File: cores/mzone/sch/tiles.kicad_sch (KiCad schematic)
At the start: 38 parts

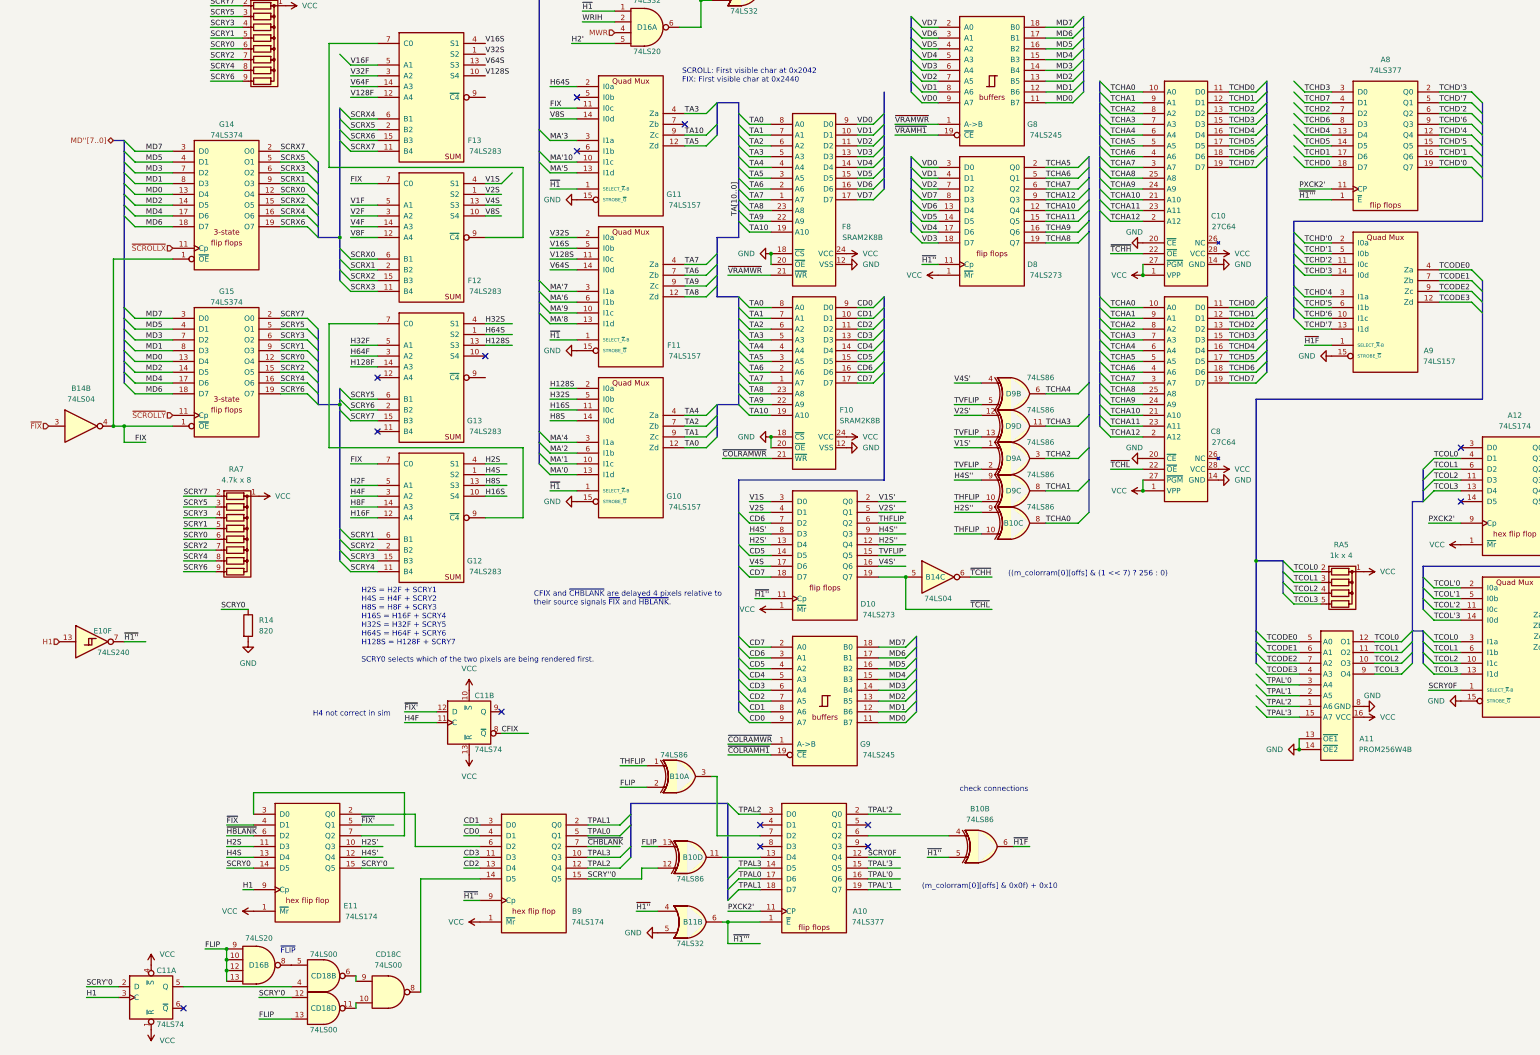
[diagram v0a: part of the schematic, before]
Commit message: mzone core
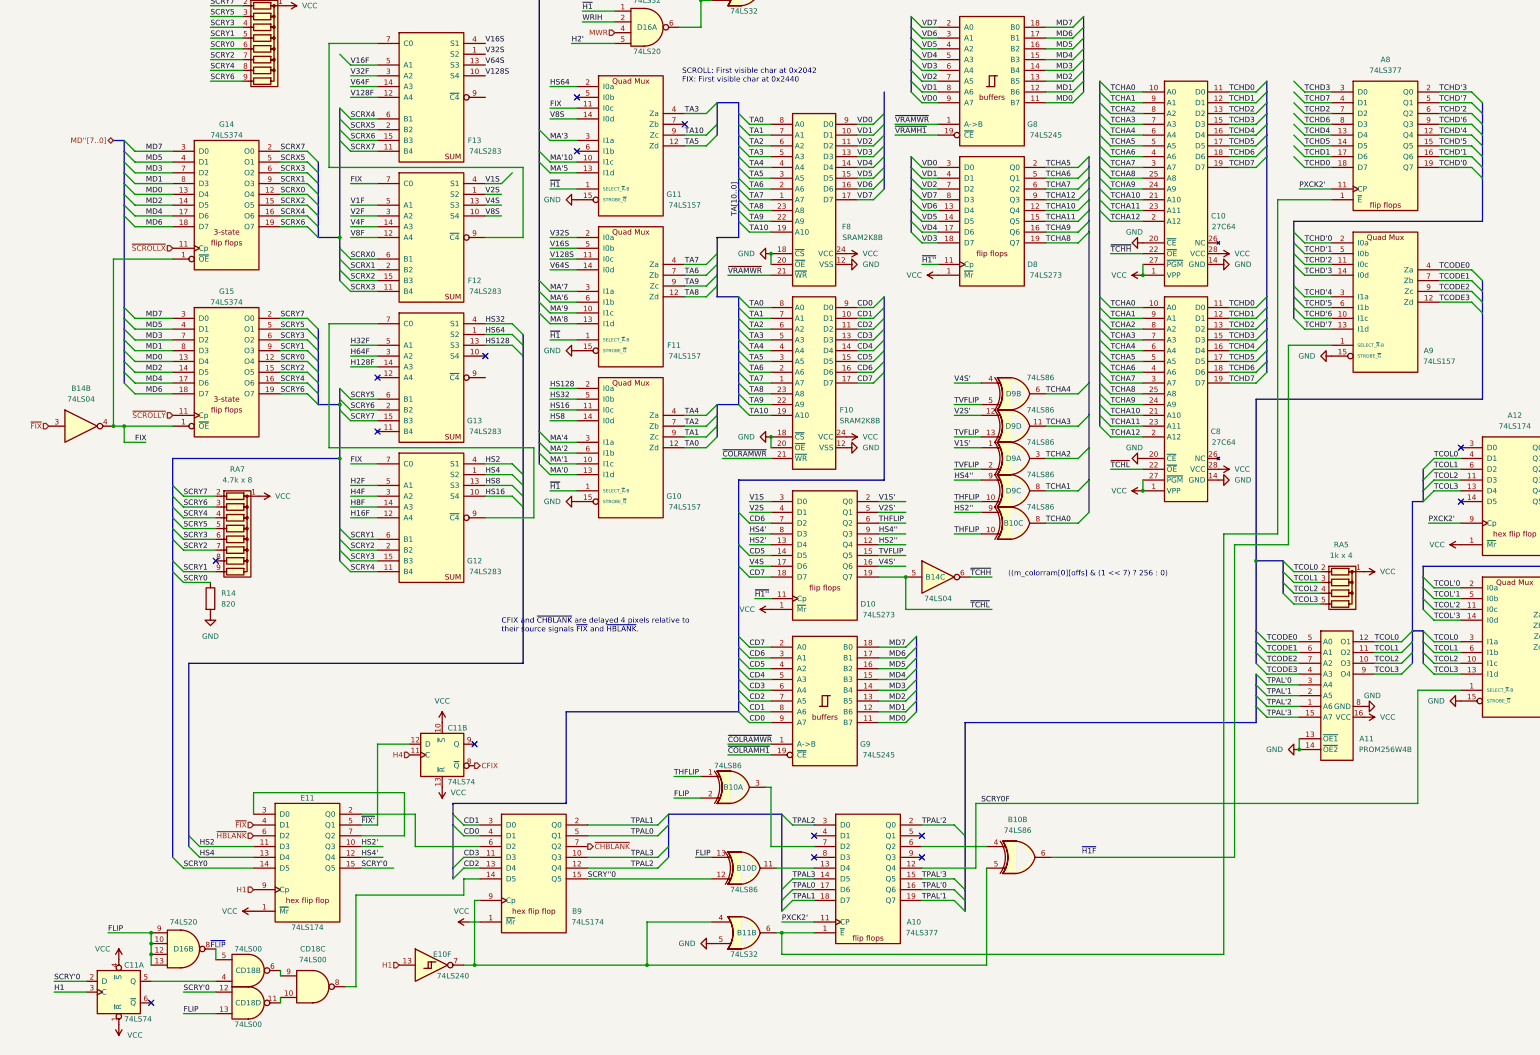
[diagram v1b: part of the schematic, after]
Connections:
- net H4F: no longer C11.11 (C)
- net SCRY0: no longer RA7.6 (R5)
- net SCRY1: now also RA7.9 (R8); no longer RA7.5 (R4)
- net SCRY3: now also RA7.6 (R5); no longer RA7.4 (R3)
- net SCRY4: now also RA7.4 (R3); no longer RA7.8 (R7)
- net SCRY5: now also RA7.5 (R4); no longer RA7.3 (R2)
- net SCRY6: now also RA7.3 (R2); no longer RA7.9 (R8)
- net ~{H1''}: no longer B10.5, B11.4, B9.9 (Cp), E10.7
- net H128S renamed HS128
- net H16S renamed HS16
- net H2S renamed HS2
- net H2S' renamed HS2'
- net H2S'' renamed HS2''
- net H32S renamed HS32
- net H4S renamed HS4
- net H4S' renamed HS4'
- net H4S'' renamed HS4''
- net H64S renamed HS64
- net H8S renamed HS8
- net ~{H1'''}: no longer names the net of A10.1 (~{E}), A8.1 (~{E}), B11.6
- net ~{H1F}: no longer names the net of A9.1 (SELECT_~{A}-B), B10.6
- new net: B10.5, B11.4, B9.9 (Cp), E10.7
- new net H4: C11.11 (C)
- no-connect marks 16 -> 17
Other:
- note added: "~{H1F}"
- note removed: "(m_colorram[0][offs] & 0x0f) + 0x10"
- note removed: "H2S = H2F + SCRY1 H4S = H4F + SCRY2 H8S = H8F + SCRY3 H16S = H16F + SCRY4 H32S = H32F + SCRY5 H64S = H64F + SCRY6 H128S = H128F + SCRY7 SCRY0 selects which of the two pixels are being rendered first."
- note removed: "H4 not correct in sim"
- note removed: "check connections"
- moved on the sheet: A10, B10A, B10B, B10D, B11B, C11A, C11B, CD18B, CD18C, CD18D, D16B, E10F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

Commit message: mzone core
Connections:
- net SCRX0: now also RA6.6 (R5)
- net SCRX1: now also RA6.5 (R4)
- net SCRX2: now also RA6.7 (R6)
- net SCRX3: now also RA6.4 (R3)
- net SCRX4: now also RA6.8 (R7)
- net SCRX5: now also RA6.3 (R2)
- net SCRX6: now also RA6.9 (R8)
- net SCRX7: now also RA6.2 (R1)
- net SCRY0: no longer RA6.6 (R5)
- net SCRY1: no longer RA6.5 (R4)
- net SCRY2: no longer RA6.7 (R6)
- net SCRY3: no longer RA6.4 (R3)
- net SCRY4: no longer RA6.8 (R7)
- net SCRY5: no longer RA6.3 (R2)
- net SCRY6: no longer RA6.9 (R8)
- net SCRY7: no longer RA6.2 (R1)
- net V4S: no longer F12.13 (S3)
- net H128F renamed HF128
- net H16F renamed HF16
- net H2F renamed HF2
- net H32F renamed HF32
- net H4F renamed HF4
- net H64F renamed HF64
- net H8F renamed HF8
- net V128F renamed VF128
- net V128S renamed VS128
- net V16F renamed VF16
- net V16S renamed VS16
- net V1F renamed VF1
- net V1S renamed VS1
- net V2F renamed VF2
- net V2S renamed VS2
- net V32F renamed VF32
- net V32S renamed VS32
- net V4F renamed VF4
- net V64F renamed VF64
- net V64S renamed VS64
- net V8F renamed VF8
- net V8S renamed VS8
- net ~{COLRAM'} renamed ~{CRAM'}
- net ~{COLRAMH1} renamed ~{CRAMBE}
- net ~{COLRAMWR} renamed ~{CRAMWR}
- net ~{VRAMH1} renamed ~{VRAMBE}
- new net VS4: F12.13 (S3)
- no-connect marks 17 -> 19
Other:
- note removed: "((m_colorram[0][offs] & (1 << 7) ? 256 : 0)"
- moved on the sheet: A8, A9, B10A, B10C, B14C, C10, C11B, C8, D10, D16A, D17A, D17B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

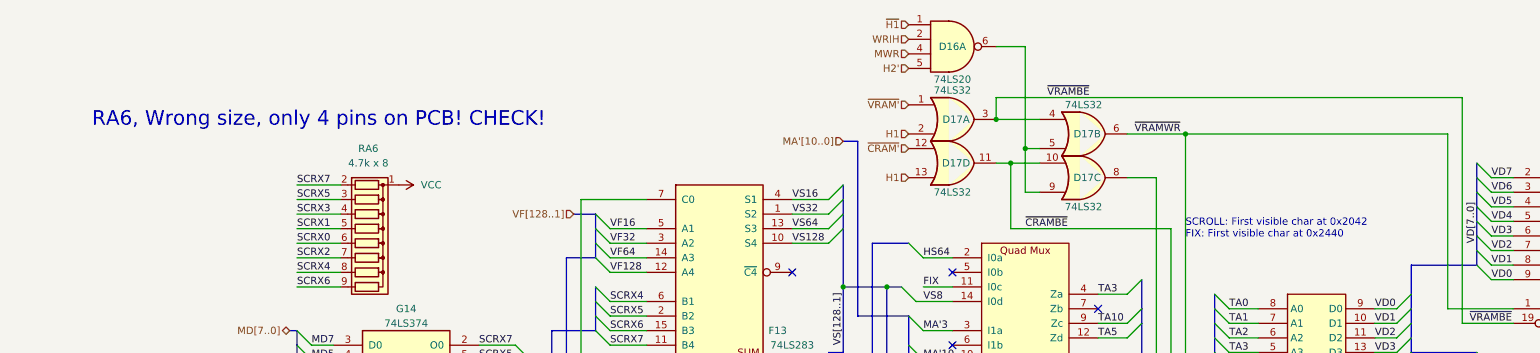
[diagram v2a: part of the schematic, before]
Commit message: mzone core
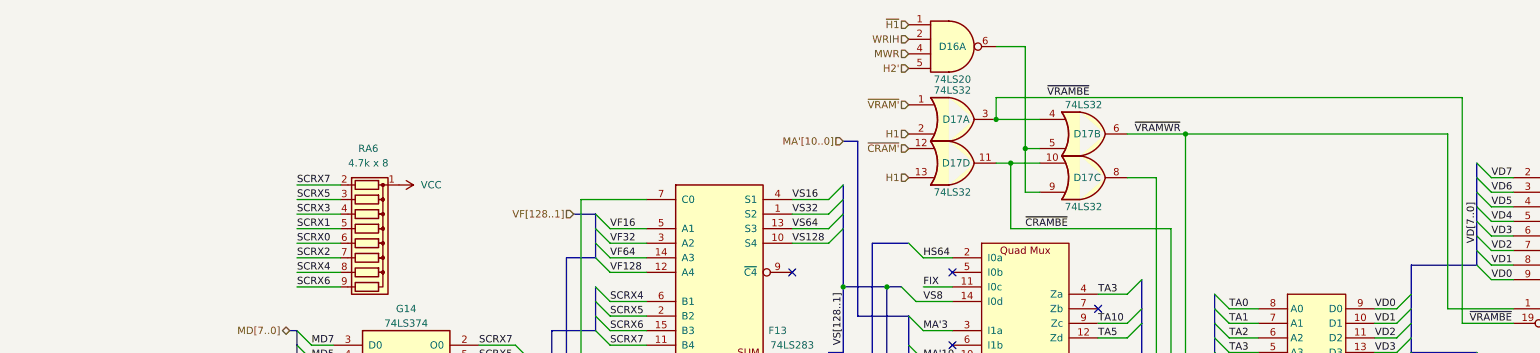
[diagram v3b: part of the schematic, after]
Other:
- note removed: "RA6, Wrong size, only 4 pins on PCB! CHECK!"
- note removed: "SCROLL: First visible char at 0x2042 FIX: First visible char at 0x2440"

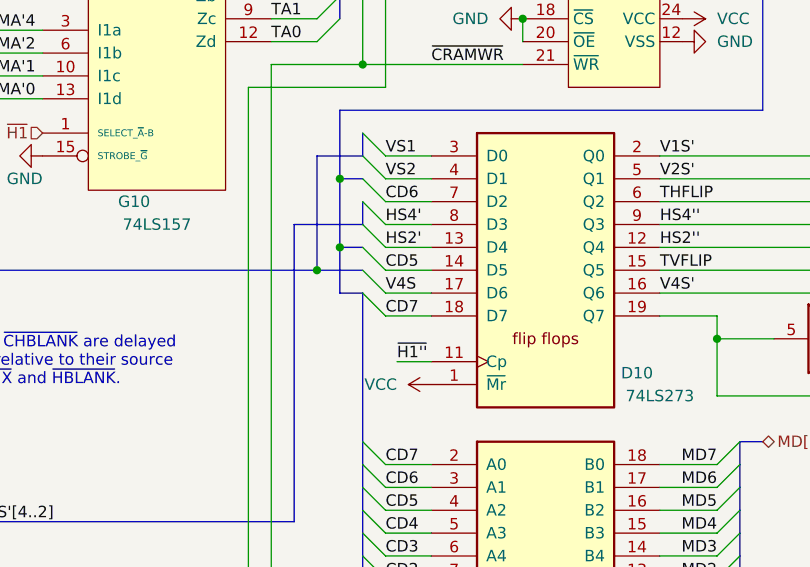
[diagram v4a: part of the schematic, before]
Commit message: mzone core
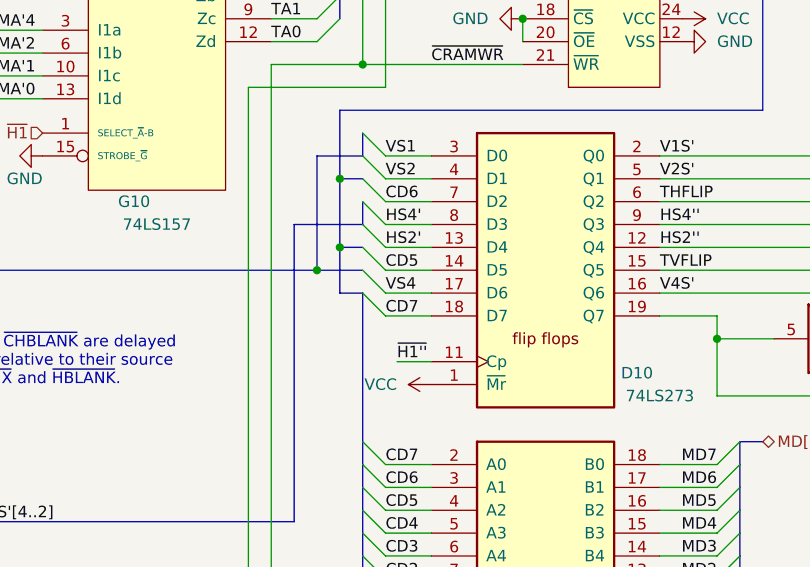
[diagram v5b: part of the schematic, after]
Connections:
- net V4S is gone; now on net VS4: D10.17 (D6)

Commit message: mzone core
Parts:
- added unit 5 of B10
- added unit 5 of B11
- added unit 7 of B14
- added unit 3 of C11
- added unit 5 of CD18
- added unit 3 of D16
- added unit 5 of D17
- added unit 5 of D9
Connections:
- net VSS is gone; now on net GND: A12.8 (VSS), B9.8 (VSS), E11.8 (VSS)
- net GND: now also B10.7 (GND), B11.7 (GND), B14.7 (GND), C11.7 (GND), CD18.7 (GND), D16.7 (GND), D17.7 (GND), D9.7 (GND)
- net VCC: now also B10.14 (VCC), B11.14 (VCC), B14.14 (VCC), C11.14 (VCC), CD18.14 (VCC), D16.14 (VCC), D17.14 (VCC), D9.14 (VCC)
- net ~{H1''}: no longer D10.11 (Cp)
- net at B10.5, B11.4, B9.9 (Cp)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: now also D10.11 (Cp)
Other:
- moved on the sheet: A12, B10A, B10D

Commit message: mzone core
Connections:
- net ~{H1''} is gone; now on net ~{HT1}: D8.11 (Cp)
- net ~{HT1}: now reaches B10.5, B11.4, B9.9 (Cp), D10.11 (Cp), E10.7
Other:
- moved on the sheet: B14C

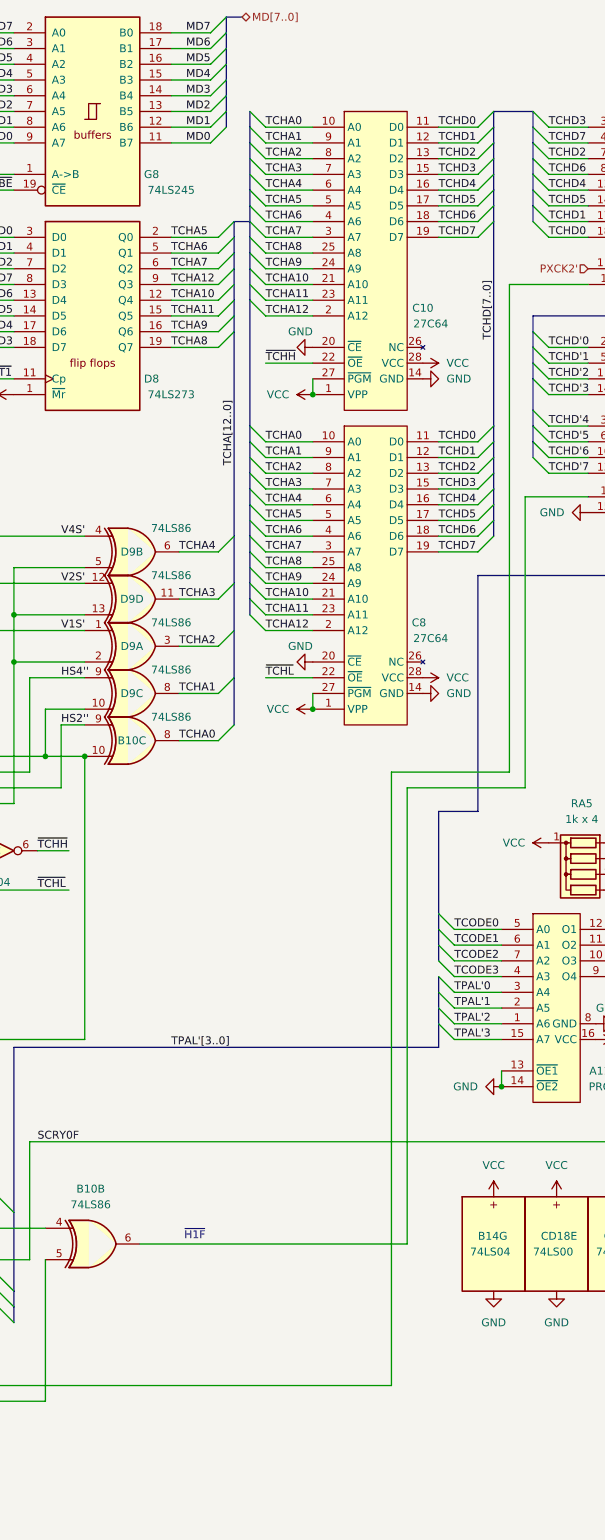
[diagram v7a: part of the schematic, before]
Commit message: mzone core
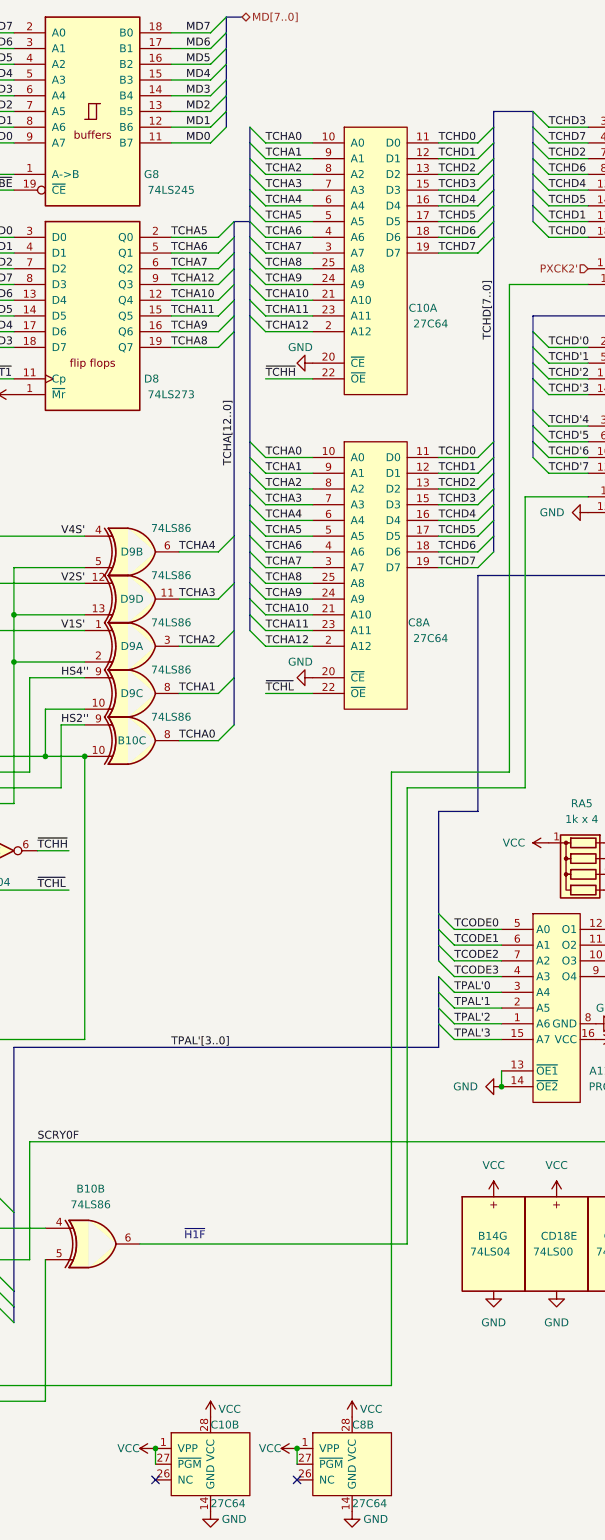
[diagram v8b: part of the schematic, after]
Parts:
- added unit 2 of C10
- added unit 2 of C8
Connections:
- net GND: now also C10.14 (GND), C8.14 (GND); no longer C10.14 (GND), C8.14 (GND)
- net VCC: now also C10.1 (VPP), C10.27 (~{PGM}), C10.28 (VCC), C8.1 (VPP), C8.27 (~{PGM}), C8.28 (VCC); no longer C10.1 (VPP), C10.27 (~{PGM}), C10.28 (VCC), C8.1 (VPP), C8.27 (~{PGM}), C8.28 (VCC)
- no-connect marks 19 -> 21
